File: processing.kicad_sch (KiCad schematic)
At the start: 47 parts, among them IC4 MT29F2G01ABAGDWB-IT_G_TR, IC5 MT29F2G01ABAGDWB-IT_G_TR, IC6 XMC7200D-E272K8384AA, IC7 DS90LV011AHMF_NOPB, Q1 ZXT849K, Y1 DSC1101DM2-012.0000

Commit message: Testpads everywhere; passives' footprints updated from MDE components; bigger DC_IN pads
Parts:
- added TP10: QSPI_SEL0, TestPoint:TestPoint_Pad_2.0x2.0mm, symbol Connector:TestPoint
- added TP11: QSPI_IO1, TestPoint:TestPoint_Pad_2.0x2.0mm, symbol Connector:TestPoint
- added TP12: QSPI_IO2, TestPoint:TestPoint_Pad_2.0x2.0mm, symbol Connector:TestPoint
- added TP13: QSPI_IO3, TestPoint:TestPoint_Pad_2.0x2.0mm, symbol Connector:TestPoint
- added TP14: QSPI_SCLK, TestPoint:TestPoint_Pad_2.0x2.0mm, symbol Connector:TestPoint
- added TP15: QSPI_IO0, TestPoint:TestPoint_Pad_2.0x2.0mm, symbol Connector:TestPoint
- added TP16: DRV_VOUT, TestPoint:TestPoint_Pad_2.0x2.0mm, symbol Connector:TestPoint
- added TP17: QSPI_SEL1, TestPoint:TestPoint_Pad_2.0x2.0mm, symbol Connector:TestPoint
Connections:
- net DRV_VOUT: now also TP16.1
- net QSPI_IO0: now also TP15.1
- net QSPI_IO1: now also TP11.1
- net QSPI_IO2: now also TP12.1
- net QSPI_IO3: now also TP13.1
- net QSPI_SCLK: now also TP14.1
- net QSPI_SEL0: now also TP10.1
- net QSPI_SEL1: now also TP17.1

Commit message: Lots of small changes
Some power and ground planes need to be looked at
All parts need to be reexamined before ordering
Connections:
- net SWJ_TRSTN: now reaches IC6.A14 (P2.0)
- net SCB8_RX: now reaches IC6.R1 (P12.0)
- net SCB8_TX: now reaches IC6.R2 (P12.1)
- net SCB8_RTS: now reaches IC6.R3 (P12.2)
- net SCB8_CTS: now reaches IC6.T1 (P12.3)
- net SCB3_CTS: now reaches IC6.T15 (P17.4)
- net SCB3_RTS: now reaches IC6.U15 (P17.3)
- net JTAG_SWCLK (P23.5) renamed SWJ_SWCLK_TCLK
- net JTAG_SWDIO (P23.6) renamed SWJ_SWDIO_TMS
- net JTAG_SWO (P23.4) renamed SWJ_SWO_TDO
- net JTAG_TDI (P23.7) renamed SWJ_SWDOE_TDI
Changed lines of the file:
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@@
+		)
+	)
+	(hierarchical_label "SCB3_CTS"
+		(shape bidirectional)
+		(at 389.89 179.07 0)
+		(effects
+			(font
+				(size 1.27 1.27)
+			)
+			(justify left)
 		)
 	)
@@
 		)
 	)
-	(hierarchical_label "JTAG_TDI (P23.7)"
+	(hierarchical_label "SWJ_SWDOE_TDI"
 		(shape input)
 		(at 191.77 184.15 180)
@@
 		)
 	)
+	(hierarchical_label "SCB8_RX"
+		(shape bidirectional)
+		(at 316.23 285.75 270)
+		(effects
+			(font
+				(size 1.27 1.27)
+			)
+			(justify right)
+		)
+	)
 	(hierarchical_label "ETH0_REF_CLK (P18.0)"
 		(shape output)
@@
 		)
 	)
-	(hierarchical_label "JTAG_SWDIO (P23.6)"
+	(hierarchical_label "SWJ_SWDIO_TMS"
 		(shape bidirectional)
 		(at 191.77 186.69 180)
@@
 		)
 	)
+	(hierarchical_label "SWJ_TRSTN"
+		(shape bidirectional)
+		(at 312.42 123.19 90)
+		(effects
+			(font
+				(size 1.27 1.27)
+			)
+			(justify left)
+		)
+	)
 	(hierarchical_label "+3V3"
 		(shape input)
@@
 		)
 	)
+	(hierarchical_label "SCB8_TX"
+		(shape bidirectional)
+		(at 318.77 285.75 270)
+		(effects
+			(font
+				(size 1.27 1.27)
+			)
+			(justify right)
+		)
+	)
 	(hierarchical_label "CMOS_CLK_OUT"
 		(shape input)
@@
 		)
 	)
+	(hierarchical_label "SCB3_RTS"
+		(shape bidirectional)
+		(at 389.89 224.79 0)
+		(effects
+			(font
+				(size 1.27 1.27)
+			)
+			(justify left)
+		)
+	)
 	(hierarchical_label "CMOS_SPI_EN (P7.3)"
 		(shape bidirectional)
@@
 		)
 	)
-	(hierarchical_label "JTAG_SWCLK (P23.5)"
+	(hierarchical_label "SWJ_SWCLK_TCLK"
 		(shape input)
 		(at 191.77 204.47 180)
@@
 		)
 	)
-	(hierarchical_label "JTAG_SWO (P23.4)"
+	(hierarchical_label "SWJ_SWO_TDO"
 		(shape input)
 		(at 191.77 207.01 180)
 		(effects
 			(font
+				(size 1.27 1.27)
+			)
+			(justify right)
+		)
+	)
+	(hierarchical_label "SCB8_CTS"
+		(shape bidirectional)
+		(at 389.89 143.51 0)
+		(effects
+			(font
+				(size 1.27 1.27)
+			)
+			(justify left)
+		)
+	)
+	(hierarchical_label "SCB8_RTS"
+		(shape bidirectional)
+		(at 321.31 285.75 270)
+		(effects
+			(font

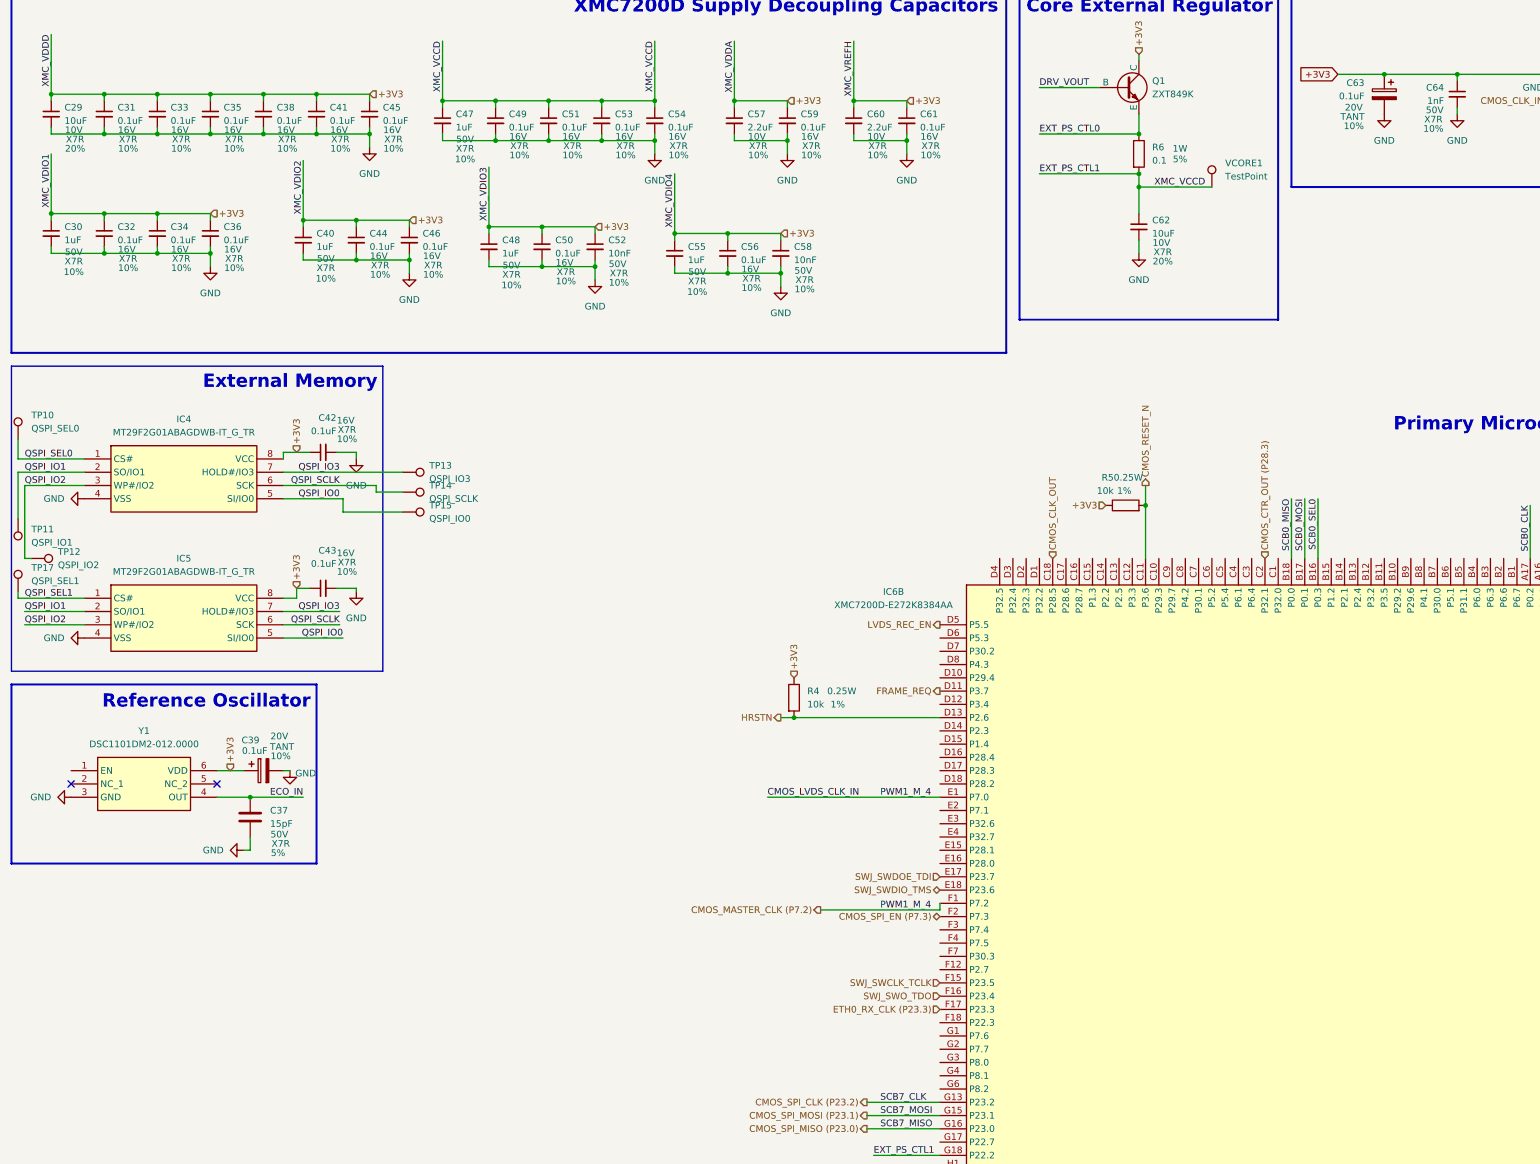
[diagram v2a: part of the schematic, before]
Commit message: Almost done
Taking a break and making a push. Known things to do:
Add pull-up resistors to ETH MDIO, ETH MDC, and XRESL.
Source a 100uF capacitor for primary regulator.
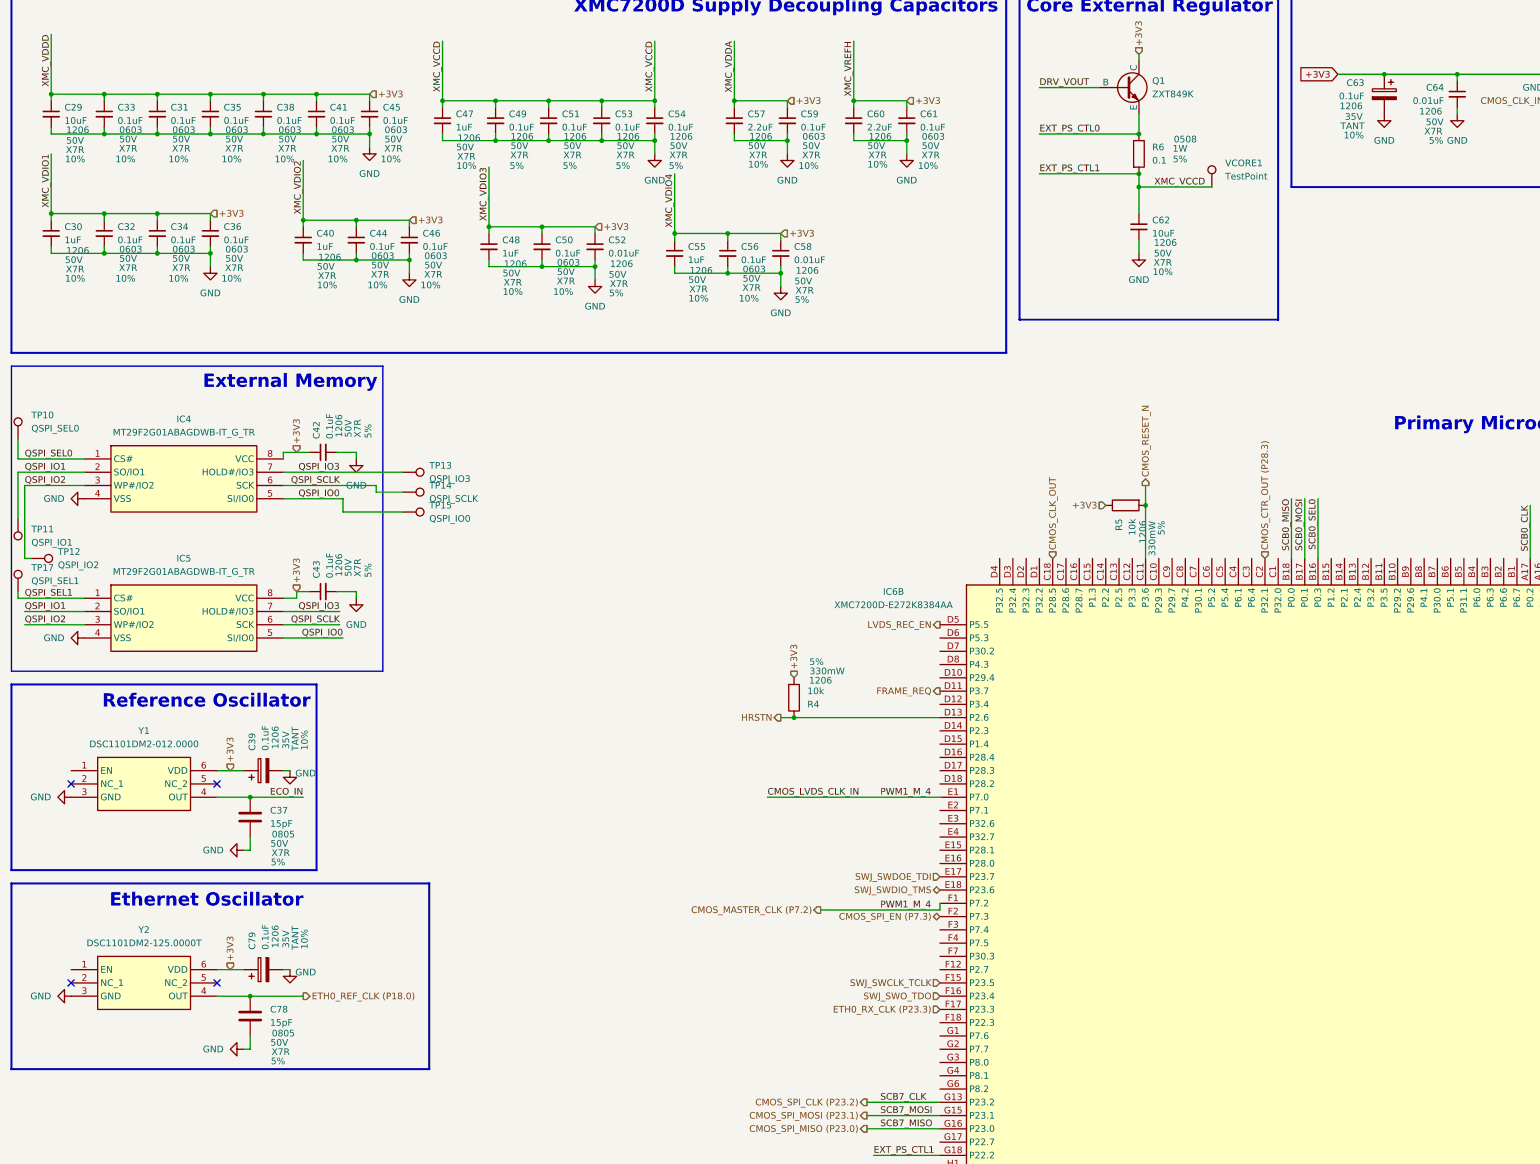
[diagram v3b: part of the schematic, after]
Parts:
- added C78: 15pF, Capacitor_SMD:C_0805_2012Metric, symbol Device:C
- added C79: 0.1uF, Capacitor_SMD:C_1206_3216Metric, symbol Device:C_Polarized
- added Y2: DSC1101DM2-125.0000T, SamacSys_Parts:DSC1101DM20120000, symbol SamacSys_Parts:DSC1101DM2-012.0000
- C29, C62: footprint Capacitor_SMD:C_0603_1608Metric -> Capacitor_SMD:C_1206_3216Metric; Mouser Part Number 81-GRM188Z71A106MA3J -> 187-CL31B106KBK6PJE; Mouser Price/Stock https://www.mouser.com/ProductDetail/Murata-Electronics/GRM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 -> https://www.mouser.com/ProductDetail/Samsung-Electro-Mechan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; Package Size (none) -> 1206; Tolerance 20% -> 10%; Voltage Rating 10V -> 50V
- C30, C40, C47, C48, C55: footprint Capacitor_SMD:C_0603_1608Metric -> Capacitor_SMD:C_1206_3216Metric; Mouser Part Number 963-MLASU168AB7105KT -> 963-UMK316B7105KL-T; Mouser Price/Stock https://www.mouser.com/ProductDetail/TAIYO-YUDEN/MLASU168AB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 -> https://www.mouser.com/ProductDetail/TAIYO-YUDEN/UMK316B710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; Package Size (none) -> 1206
- C31, C32, C33, C34, C35, C36, C38, C41, C44, C45, C46, C50, C56, C59, C61: Mouser Part Number 81-GCM188R71C104KA7J -> 963-UMK107B7104KAHT; Mouser Price/Stock https://www.mouser.com/ProductDetail/Murata-Electronics/GCM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 -> https://www.mouser.com/ProductDetail/TAIYO-YUDEN/UMK107B710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; Package Size (none) -> 0603; Voltage Rating 16V -> 50V
- C37: footprint Capacitor_SMD:C_0603_1608Metric -> Capacitor_SMD:C_0805_2012Metric; Mouser Part Number 80-C0603C150J5RACTU -> 80-C0805C150J5RACTU; Mouser Price/Stock https://www.mouser.com/ProductDetail/KEMET/C0603C150J5RACTU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 -> https://www.mouser.com/ProductDetail/KEMET/C0805C150J5RACTU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; Package Size (none) -> 0805
- C39, C63: footprint Capacitor_SMD:C_0805_2012Metric -> Capacitor_SMD:C_1206_3216Metric; Mouser Part Number 581-TAJR104K020R -> 581-TAJA104K035SNJ; Mouser Price/Stock https://www.mouser.com/ProductDetail/KYOCERA-AVX/TAJR104K02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 -> https://www.mouser.com/ProductDetail/KYOCERA-AVX/TAJA104K03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; Package Size (none) -> 1206; Voltage Rating 20V -> 35V
- C42, C43, C49, C51, C53, C54: footprint Capacitor_SMD:C_0603_1608Metric -> Capacitor_SMD:C_1206_3216Metric; Mouser Part Number 81-GCM188R71C104KA7J -> 581-12065C104J4Z2A; Mouser Price/Stock https://www.mouser.com/ProductDetail/Murata-Electronics/GCM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 -> https://www.mouser.com/ProductDetail/KYOCERA-AVX/12065C104J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; Package Size (none) -> 1206; Tolerance 10% -> 5%; Voltage Rating 16V -> 50V
- C52, C58: value 10nF -> 0.01uF; footprint Capacitor_SMD:C_0603_1608Metric -> Capacitor_SMD:C_1206_3216Metric; Mouser Part Number 81-GCM188R71H103KA7J -> 581-12065C103J4T4A; Mouser Price/Stock https://www.mouser.com/ProductDetail/Murata-Electronics/GCM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 -> https://www.mouser.com/ProductDetail/KYOCERA-AVX/12065C103J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; Package Size (none) -> 1206; Tolerance 10% -> 5%
- C57, C60: footprint Capacitor_SMD:C_0603_1608Metric -> Capacitor_SMD:C_1206_3216Metric; Mouser Part Number 963-LMK107B7225KA-TR -> 80-C1206X225K5REAULR; Mouser Price/Stock https://www.mouser.com/ProductDetail/TAIYO-YUDEN/LMK107B722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 -> https://www.mouser.com/ProductDetail/KEMET/C1206X225K5RECAU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; Package Size (none) -> 1206; Voltage Rating 10V -> 50V
- C64: value 1nF -> 0.01uF; footprint Capacitor_SMD:C_0603_1608Metric -> Capacitor_SMD:C_1206_3216Metric; Mouser Part Number 581-KAM15AR71H102KM -> 581-12065C103J4T4A; Mouser Price/Stock https://www.mouser.com/ProductDetail/KYOCERA-AVX/KAM15AR71H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 -> https://www.mouser.com/ProductDetail/KYOCERA-AVX/12065C103J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; Package Size (none) -> 1206; Tolerance 10% -> 5%
- R4, R5: Mouser Part Number 71-CRCW060310K0FKEI -> 667-ERJ-T08J103V; Mouser Price/Stock https://www.mouser.com/ProductDetail/Vishay-Dale/CRCW060310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 -> https://www.mouser.com/ProductDetail/Panasonic/ERJ-T08J103V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; Package Size (none) -> 1206; Power Rating 0.25W -> 330mW; Tolerance 1% -> 5%
- R6: Package Size (none) -> 0508
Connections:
- net +3V3: now also R4.2, C79.1, Y2.6 (VDD); no longer R4.1
- net ETH0_REF_CLK (P18.0): now also C78.1, Y2.4 (OUT)
- net GND: now also C78.2, C79.2, Y2.3 (GND)
- net HRSTN: now also R4.1; no longer R4.2
- no-connect marks 2 -> 4
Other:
- note added: "Ethernet Oscillator"
